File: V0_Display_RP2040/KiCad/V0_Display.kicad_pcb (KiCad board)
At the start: 2 copper layers, 80 x 35 mm, 43 parts, among them J1 GPIO, J2 I2C Header, J3 SWD, J4 USB4105-GF-A, J7 USB_Header, J8 Neopixel, SW6 Kill_SW, SW7 Rotary_Enc, U1 AP2127K-3.3, U2 W25Q16JVUXIQ, U3 74LVC1G17, U4 RP2040, Y1 12MHz

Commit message: Fix Footprints
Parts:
- J4: value USB4105-GF-A -> GT-USB-7010ASV; footprint footprints:USB4105-GF-A -> Connector_USB:USB_C_Receptacle_G-Switch_GT-USB-7010ASV
- R1, R11: value 10k -> 10K
- U3: footprint V0-Display:SOT-753 -> Package_TO_SOT_SMD:SOT-23-5
- moved J4 0.25 mm to (88.8, 67.2)
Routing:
- net Net-(D1-DIN): track 12.4 -> 13.4 mm, vias 1 -> 2
- net GND: track 47.9 -> 46.9 mm, vias 16 -> 15

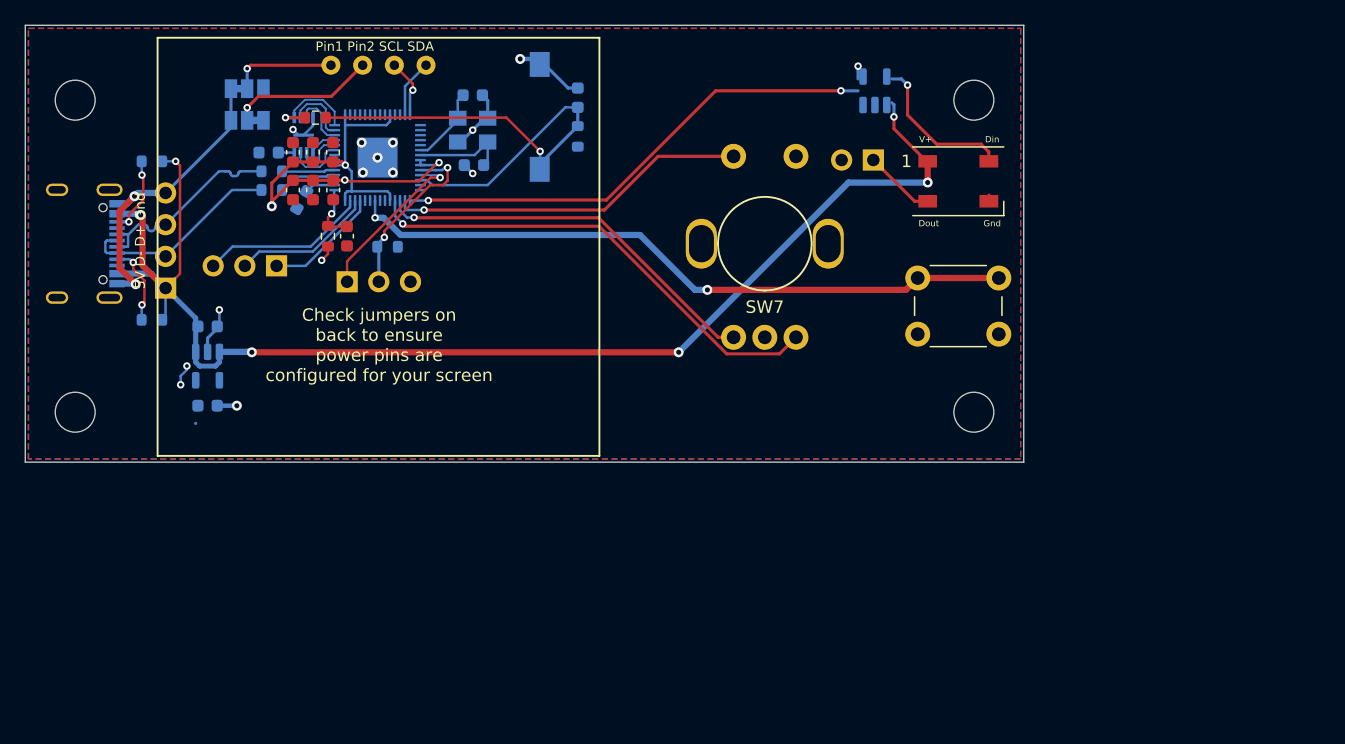
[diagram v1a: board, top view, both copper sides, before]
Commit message: Update Files
New 3.3V Regulator
"Fixed" Neopixel Level Shifter
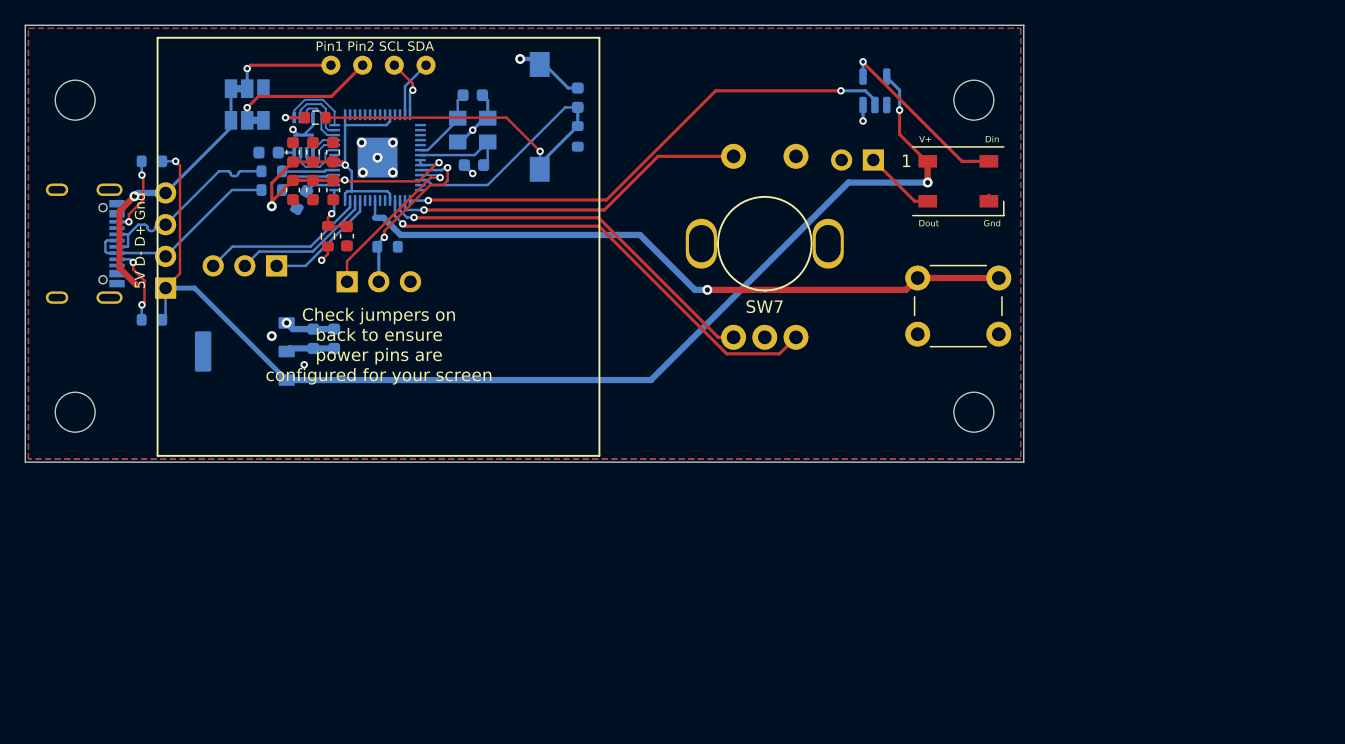
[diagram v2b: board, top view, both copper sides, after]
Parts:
- C1: value 4.7uF -> 22uF
- C2: value 4.7uF -> 0.1uF
- U1: value AP2127K-3.3 -> AMS1117-3.3; footprint Package_TO_SOT_SMD:SOT-23-5 -> footprints:AMS1117-3.3
- moved C1 10.2 mm to (109.9, 74.8), turned to 90 degrees
- moved C2 10.0 mm to (108.3, 74.8), turned to 90 degrees
- moved U1 3.21 mm to (102.8, 75.8)
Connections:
- C1 pad 1: VBUS -> +3.3V
- U1 pad 1: VBUS -> GND
- U1 pad 2: GND -> +3.3V
- U1 pad 4: unconnected-(U1-NC-Pad4) -> (no net)
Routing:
- net VBUS: track 108.9 -> 94.5 mm, vias 6 -> 3
- net GND: track 46.9 -> 40.2 mm, vias 15 -> 14
- net +3.3V: track 45.9 -> 48.8 mm
- net Neopixel: track 39.5 -> 41.2 mm
- net Net-(D1-DIN): track 13.4 -> 14.6 mm, vias 2 -> 1
- net F_PD: track 42.1 -> 41.2 mm
- net D+: track 20.8 -> 20.1 mm
- net Kill: vias 2 -> 1

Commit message: Rev 1.1
Fix Vreg-Out Problem
Change to AMS1117-3.3
22uF Input Capacitor on VBUS (5V IN)
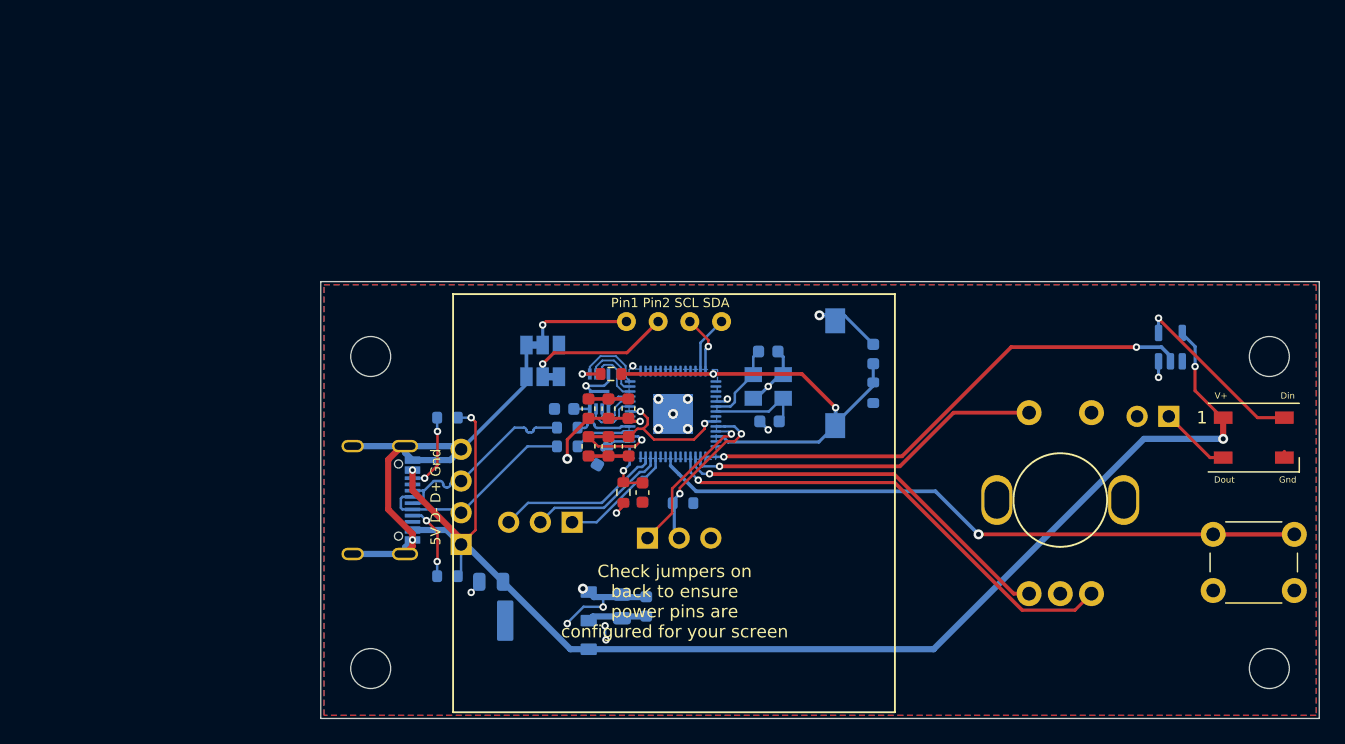
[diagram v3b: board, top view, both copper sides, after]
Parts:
- added C3: 22uF, Capacitor_SMD:C_0805_2012Metric, B.Cu at (122.5, 94.2)
- C1: footprint Capacitor_SMD:C_0603_1608Metric -> Capacitor_SMD:C_0805_2012Metric
- R2: value 1k -> 1K
- moved C2 34.2 mm to (134.9, 96.2)
- moved U1 32.4 mm to (127.0, 97.4)
- moved C10 31.6 mm to (131.4, 84.2)
- moved J3 31.6 mm to (135.0, 90.7)
- moved C1 31.5 mm to (133.0, 96.2)
- moved Y1 31.3 mm to (144.7, 78.6)
- moved J1 31.3 mm to (129.0, 89.5)
- moved R6 31.3 mm to (153.1, 79.1)
- moved R8 31.3 mm to (119.0, 81.1)
- moved C15 31.3 mm to (144.8, 81.4)
- moved C5 31.3 mm to (144.7, 75.8)
- moved C7 31.3 mm to (130.3, 83.4)
- moved C8 31.3 mm to (131.9, 83.4)
- moved C9 31.3 mm to (133.5, 83.4)
- moved D1 31.3 mm to (183.6, 82.7)
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- renumbered C16 to C4, J7 to J5, J8 to J6, R11 to R8, SW6 to SW1, SW7 to SW2
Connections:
- C7 pad 1: +3.3V -> +1V1
- C8 pad 1: +3.3V -> +1V1
- C9 pad 1: +3.3V -> +1V1
- J4 pad A1: (no net) -> GND
- J4 pad A12: (no net) -> GND
- J4 pad A4: (no net) -> VBUS
- J4 pad A6: D+ -> D27+
- J4 pad A7: D- -> D27-
- J4 pad A9: (no net) -> VBUS
- J4 pad B1: (no net) -> GND
- J4 pad B12: (no net) -> GND
- J4 pad B4: (no net) -> VBUS
- J4 pad B6: D+ -> D27+
- J4 pad B7: D- -> D27-
- J4 pad B9: (no net) -> VBUS
- J4 pad S1: (no net) -> GND
- J5 pad 2: D- -> D27-
- J5 pad 3: D+ -> D27+
- R1 pad 1: VBUS -> Net-(J4-CC1)
- R1 pad 2: Net-(J4-CC1) -> VBUS
- R4 pad 1: D+ -> D27+
- R4 pad 2: D+ -> /D+
- R5 pad 1: D- -> /D-
- R5 pad 2: D- -> D27-
- U4 pad 19: unconnected-(U4-TESTEN-Pad19) -> GND
- U4 pad 23: +3.3V -> +1V1
- U4 pad 45: +3.3V -> +1V1
- U4 pad 46: D- -> /D-
- U4 pad 47: D+ -> /D+
- U4 pad 50: +3.3V -> +1V1
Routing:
- net +3.3V: track 48.8 -> 13.4 mm, vias 5 -> 3
- net GND: track 40.2 -> 74.3 mm, vias 14 -> 19
- net D-: track 21.0 -> 0.00 mm
- net +1V1: track 0.00 -> 20.1 mm, vias 0 -> 3
- net D+: track 20.1 -> 0.00 mm
- net D27-: track 0.00 -> 16.2 mm
- net D27+: track 0.00 -> 15.8 mm
- net VBUS: track 94.5 -> 106.5 mm, vias 3 -> 4
- net F_PD: track 41.2 -> 36.1 mm, vias 1 -> 2
- net /D-: track 0.00 -> 4.71 mm
- net /D+: track 0.00 -> 4.67 mm
- net SWDCLK: track 14.0 -> 12.6 mm
- net Kill: track 54.1 -> 53.0 mm
- net SWDIO: track 13.5 -> 12.8 mm
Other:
- board text added: "+3.3V SWDCLK SWDIO"
- board text added: "27 28 29"
- board text added: "GPIO"
- board text added: "Original by Timmit99 Modified by Fisheiyy Sponsored by: Provok3d.com & Lab4450.com"
- board text added: "RP2040 V0-Display V1.1"
- board text removed: "+3.3V SWDCLK SWDIO SWD"
- board text removed: "27 28 29 GPIO"
- board text removed: "Made by Timmit99 Derived by Fisheiyy Sponsored by: Provok3d.com & Lab4450.com"
- board text removed: "RP2040 V0-Display V1"
